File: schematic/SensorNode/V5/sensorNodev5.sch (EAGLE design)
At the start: 33 parts, among them IC1 V_REG_MIC2920, J1 AVR_SPI_PRG_62X3_LOCK, U1 ATMEGA328P_TQFP, U2 ADA4077-1ARZ

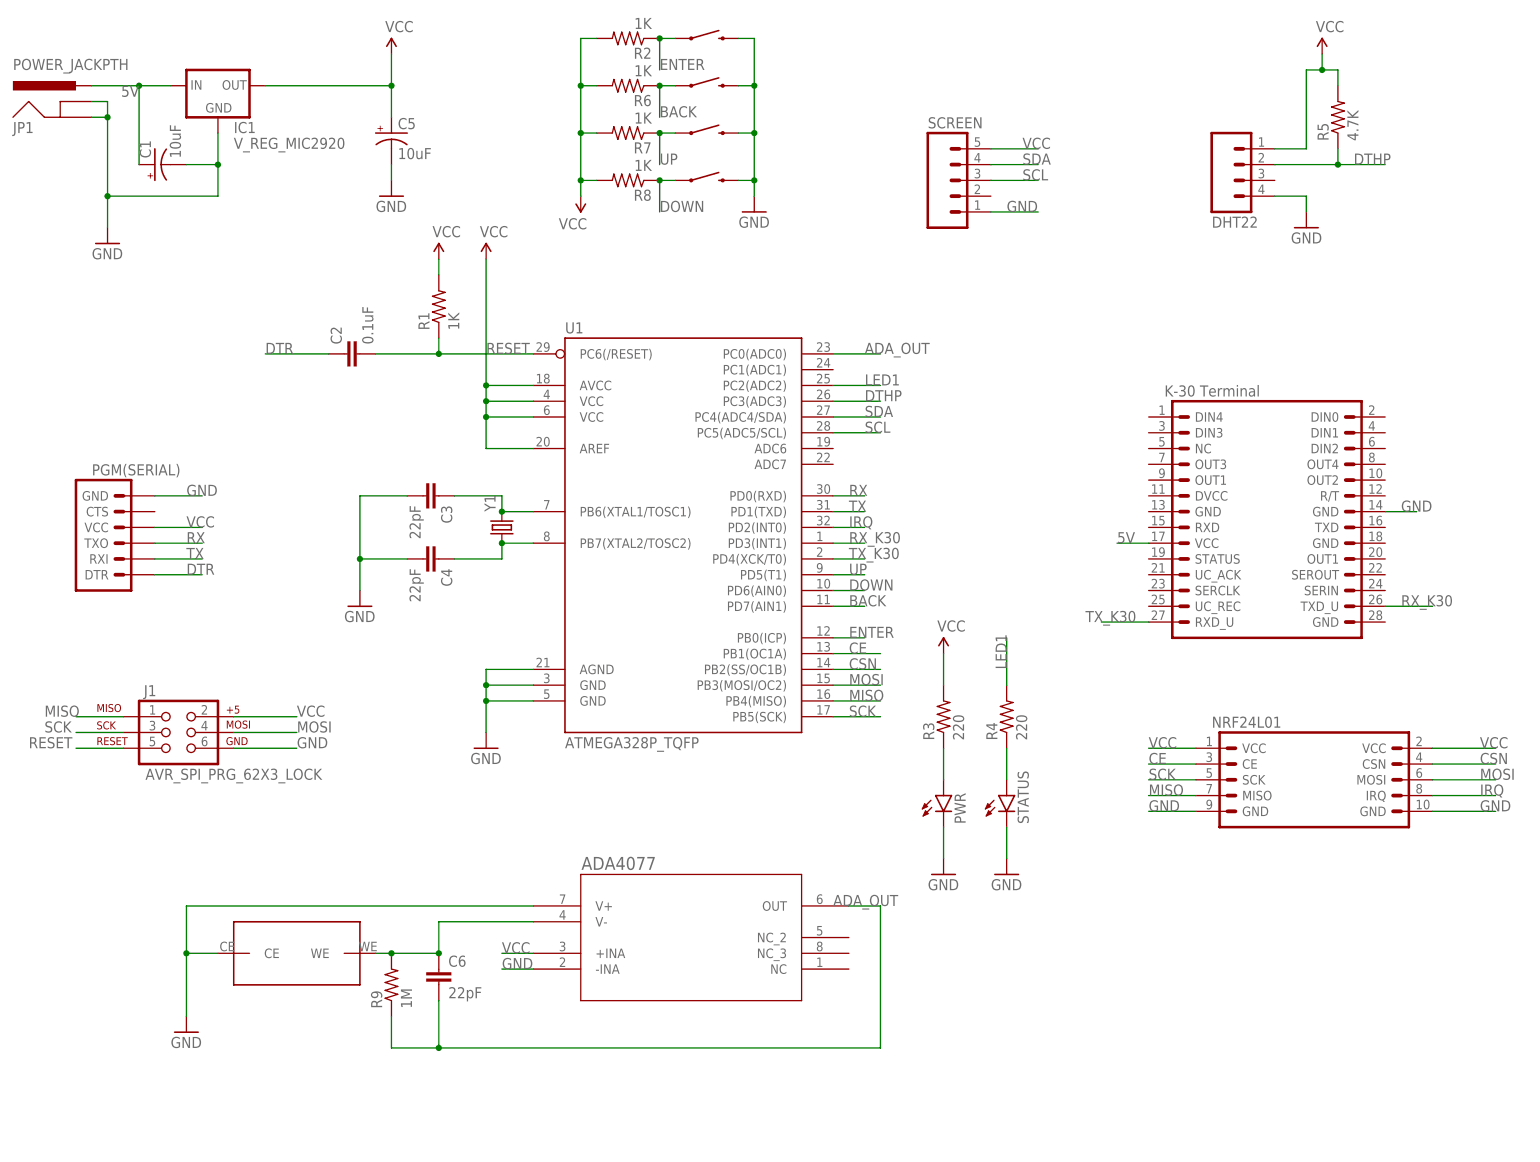
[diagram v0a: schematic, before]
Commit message: o Updated Figaro gas sensor eagle part to reflect version A00 o Fixed opamp circuit in Sensor V5 o Swapped out DHT22 for Si7021
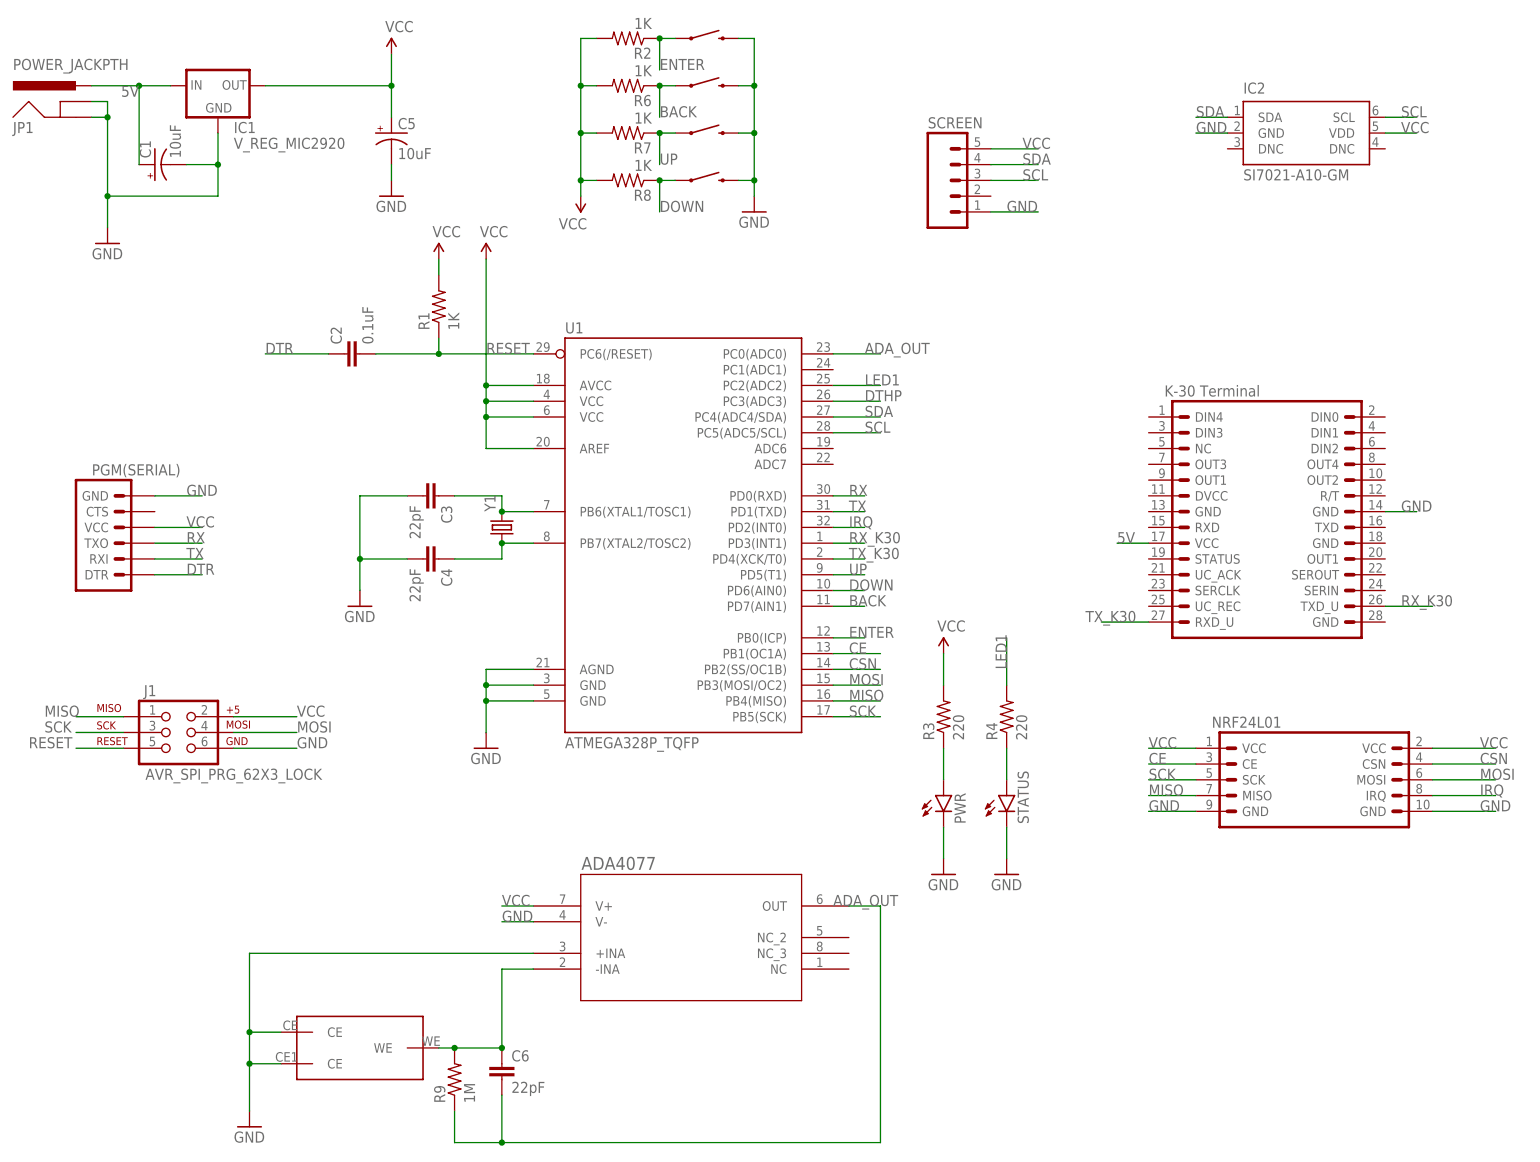
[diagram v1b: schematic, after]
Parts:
- removed DHT22: (no value), SparkFun-Connectors:M04PTH
- removed R5: 4.7K, SparkFun-Resistors:1KOHM-1/10W-1%(0603)
- added IC2: SI7021-A10-GM, bespin:SI7021-A10-GM
- JP3: device misc:K-30K-30 -> bespin:K-30K-30
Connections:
- net DTHP: no longer DHT22.2, R5.1
- net GND: now also IC2.GND, U$1.CE@1, U$1.CE@2, U2.+INA, U2.V-; no longer DHT22.4, U$1.CE, U2.-INA, U2.V+
- net N$12: now also U2.-INA; no longer U2.V-
- net SCL: now also IC2.SCL
- net SDA: now also IC2.SDA
- net VCC: now also IC2.VDD, U2.V+; no longer DHT22.1, R5.2, U2.+INA
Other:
- moved on the sheet: C6, R9
